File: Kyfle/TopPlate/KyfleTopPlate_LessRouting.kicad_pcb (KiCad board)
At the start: 2 copper layers, 164 x 146.3 mm, 38 parts, among them SW2 KEY_SWITCH, SW2 PRO MICRO

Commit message: Plates: Received M2 and M5 hardware. It's bigger than specified...
- M5 screw head is ~9.5 instead of 8.7. Was colliding in the top left 
corner with M2 screw for pro micro board. So I shifted up pro micro 
board 0.3mm.
- M2 screw head is also larger than expected (3.8 instead of 3.2). But 
it is mostly fine as I was designing with 4-4.2mm clearance. Only 
exception was for screws supporting the middle bottom section of top 
plate with rails. Here it was colliding with switch housing. So, only 
solution is to use so called reduced slotted screws (DIN 920) as they 
have 2.8mm diameter head.
- Also added JLCPCB silk reference
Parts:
- added JLCJLCJLCJLC: JLCBCB_OrderNumber, Kyfle Footprints:JLCBCB_OrderNumber, F.Cu at (226.2, 91.5)
- moved SW2 0.30 mm to (111.9, 58.4)

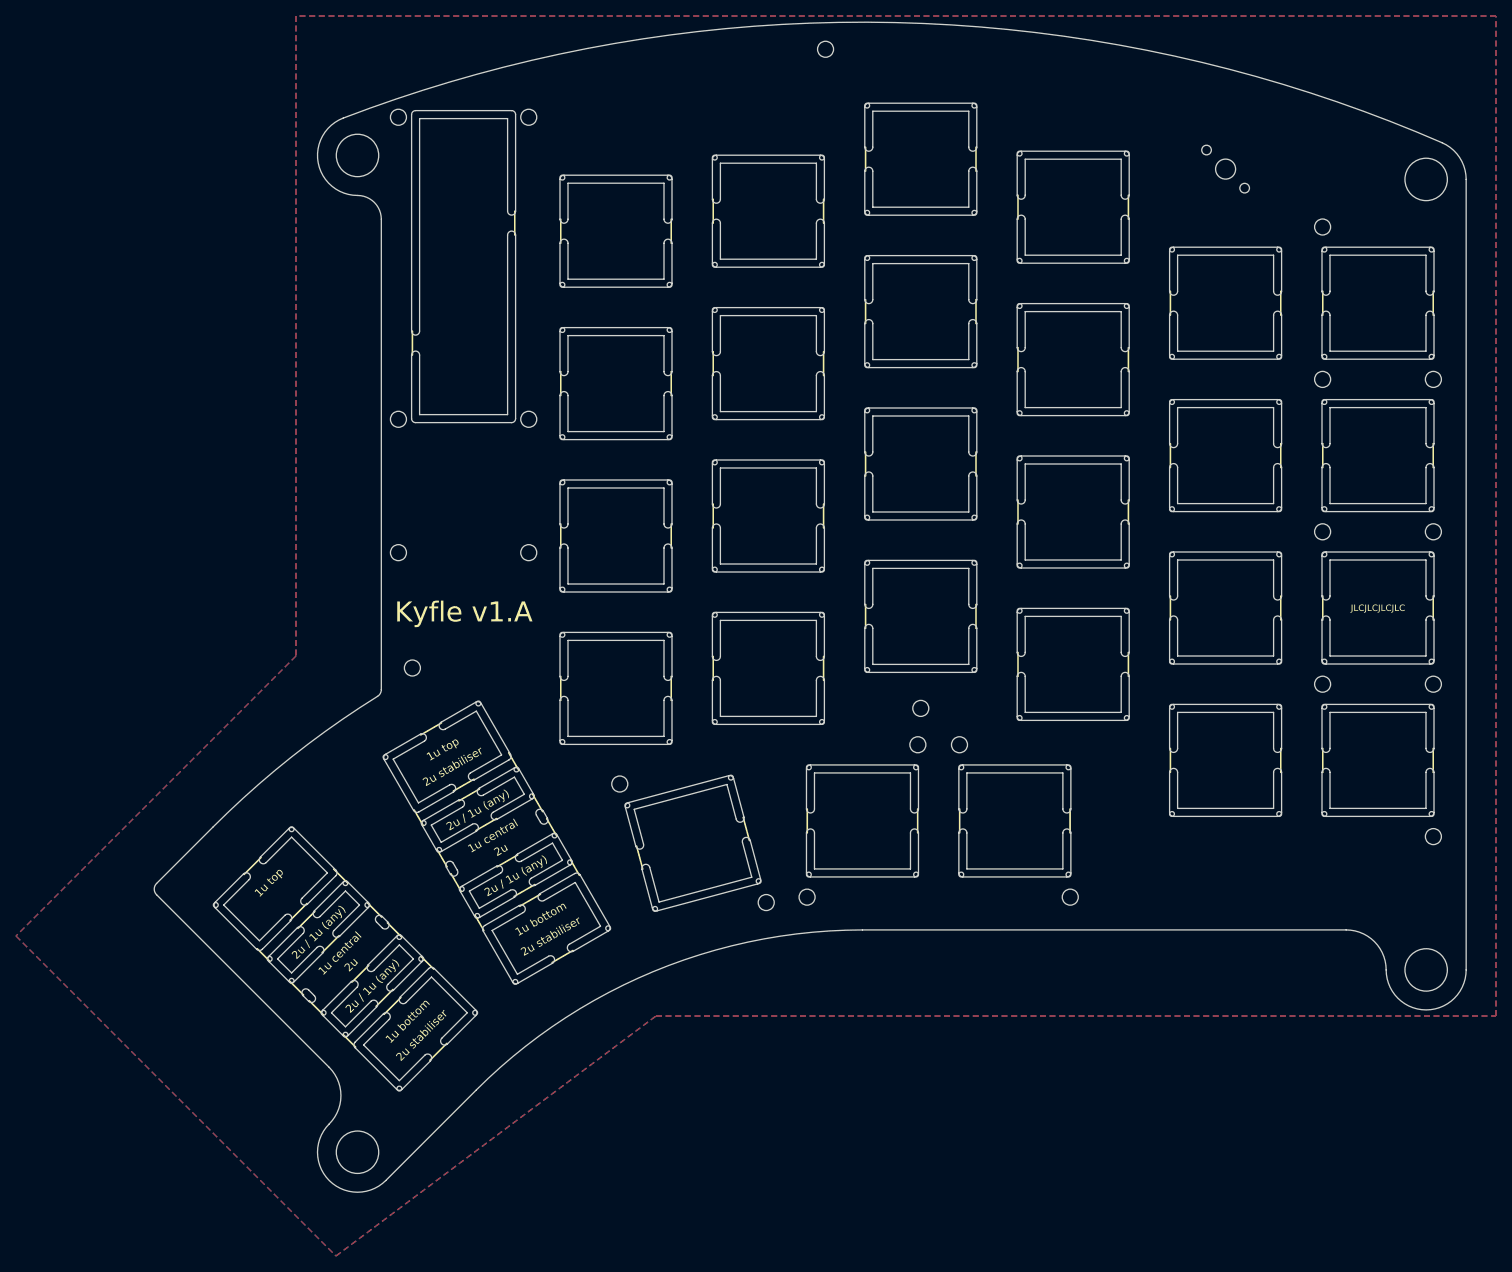
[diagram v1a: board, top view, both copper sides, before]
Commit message: Adding mouse bites to top plate (rail-less only for now)
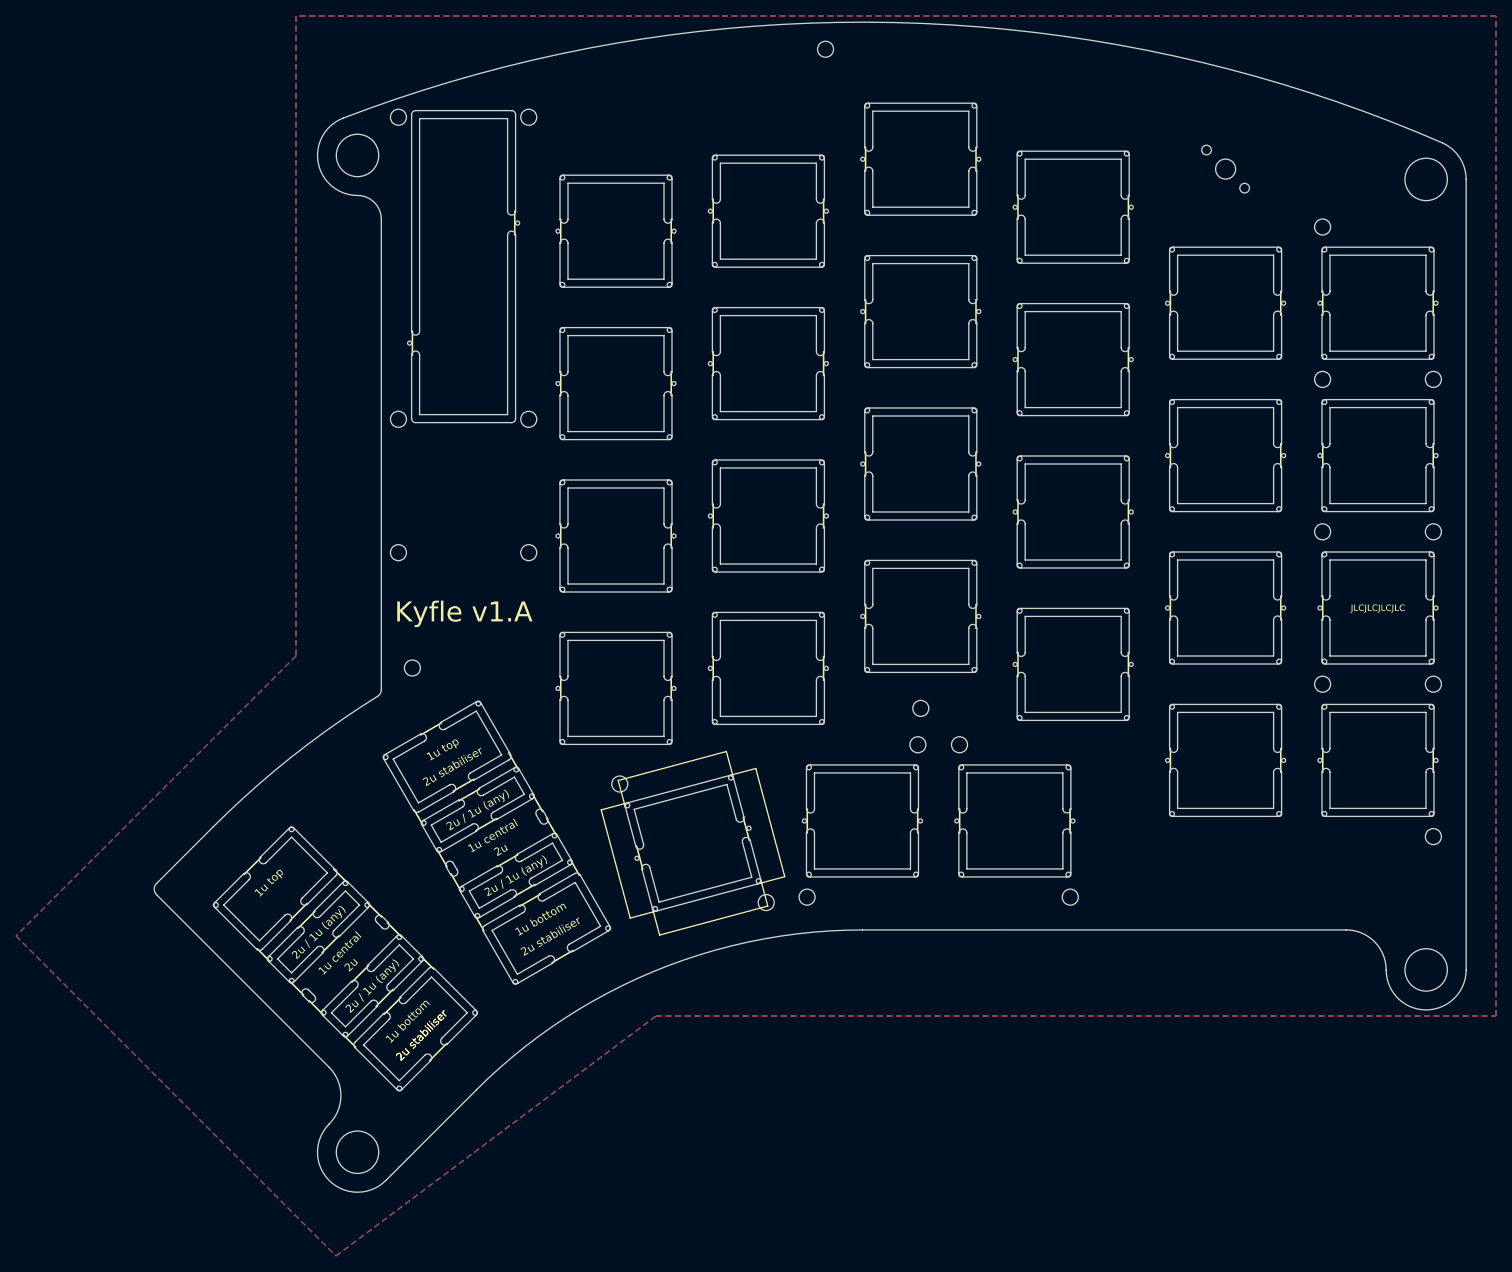
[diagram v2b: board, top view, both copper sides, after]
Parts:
- added REF**: RollerEncoder_Panasonic_EVQWGD001, Kyfle Footprints:RollerEncoder_TopPlate, F.Cu at (170.2, 152.4)

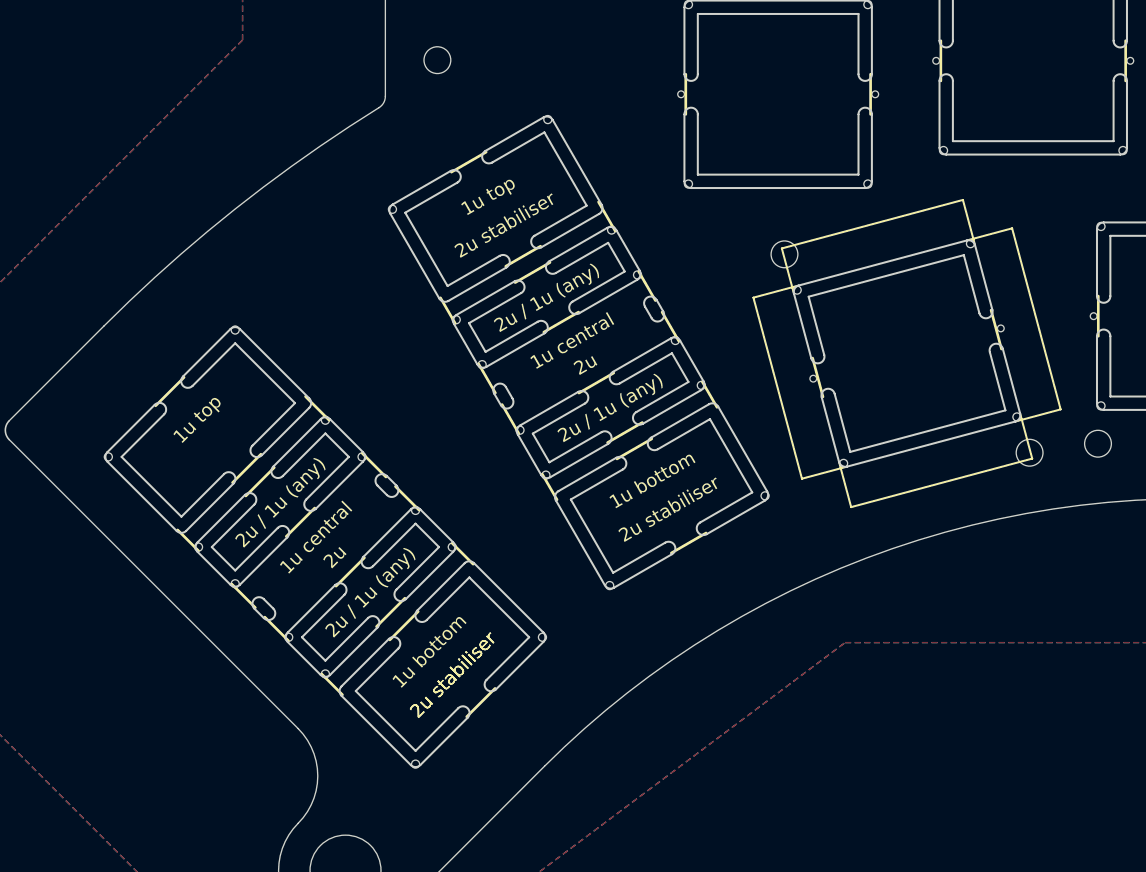
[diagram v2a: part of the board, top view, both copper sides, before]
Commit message: First attempts at supporting Pimoroni trackball
Will be further refined once I can take real measurements on them
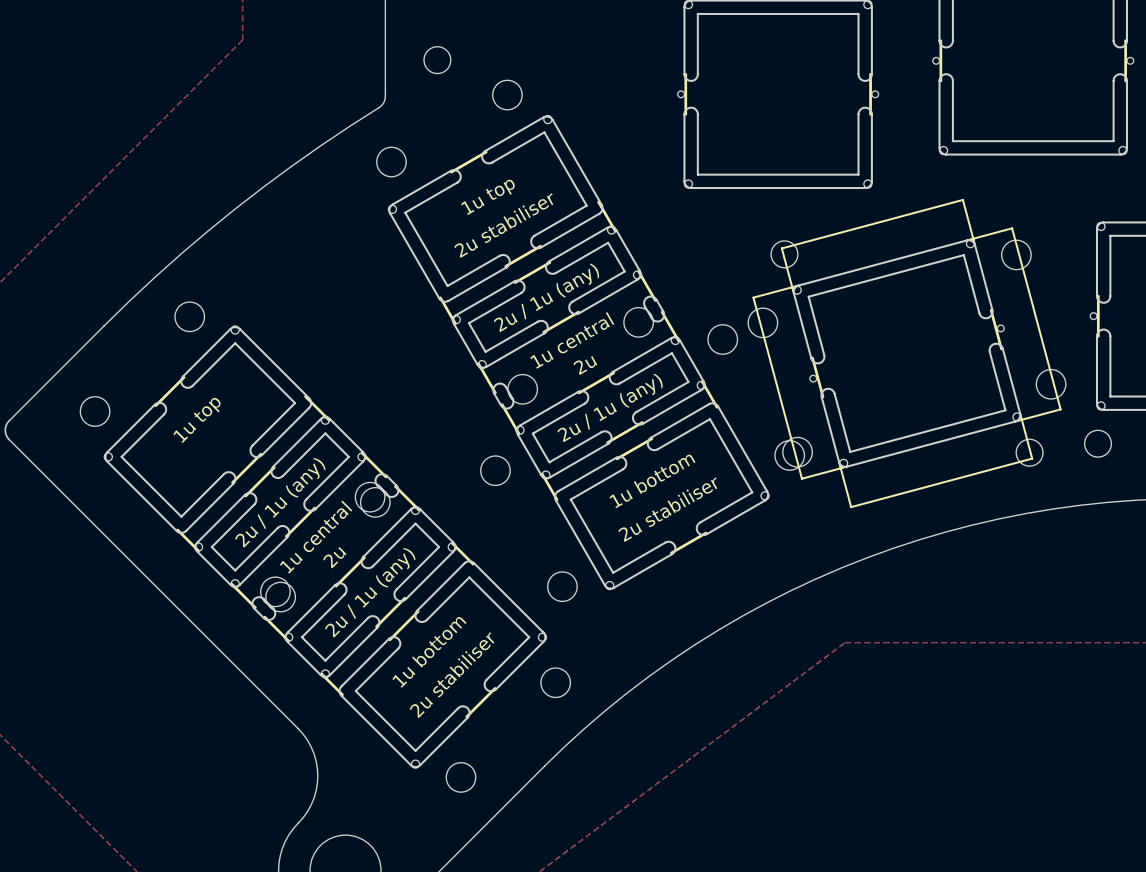
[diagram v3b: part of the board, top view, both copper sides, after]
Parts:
- added REF**: Pimonori_Trackball, Kyfle Footprints:Pimonori_Trackball, F.Cu at (90.4, 128.6)
- added REF**: Pimonori_Trackball, Kyfle Footprints:Pimonori_Trackball, F.Cu at (103.9, 142.1)
- added REF**: Pimonori_Trackball, Kyfle Footprints:Pimonori_Trackball, F.Cu at (140.6, 120.9)
- added REF**: Pimonori_Trackball, Kyfle Footprints:Pimonori_Trackball, F.Cu at (111.3, 112.6)
- added REF**: Pimonori_Trackball, Kyfle Footprints:Pimonori_Trackball, F.Cu at (120.8, 129.1)
- moved REF** 43.2 mm to (140.6, 120.9), turned to 285 degrees
